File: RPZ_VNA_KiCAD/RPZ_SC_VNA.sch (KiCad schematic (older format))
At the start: 47 parts, among them J1 GPIO Header, J2 Signal_Out, P1 Input, P2 Output, U1 SI5351A, U2 NL7WB66, U3 NL7WB66, U4 OPAMP, U5 OPAMP, Y1 CX3225

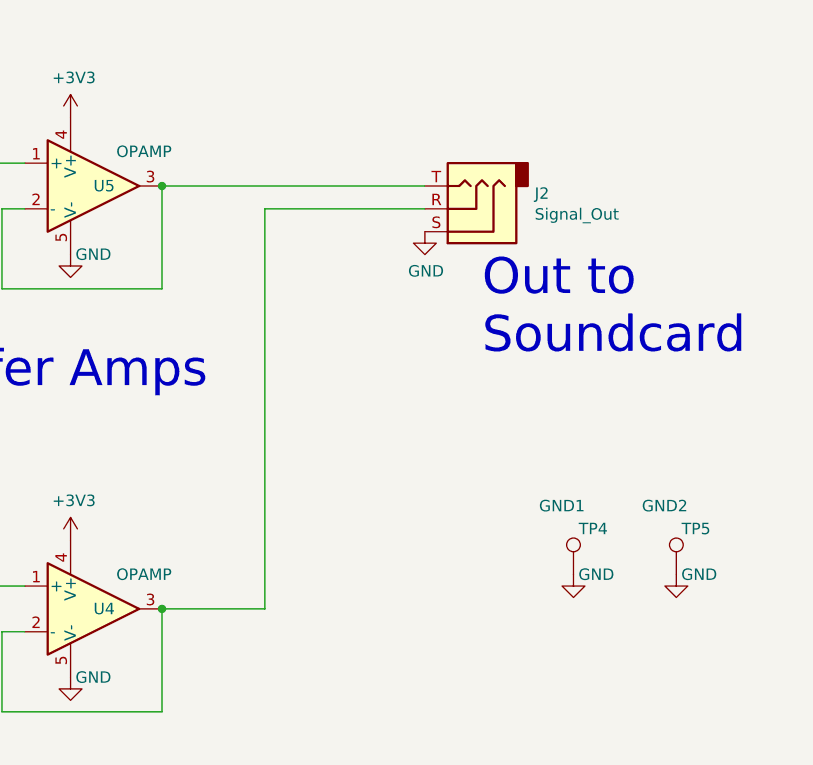
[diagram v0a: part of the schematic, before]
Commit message: Flipped Audio Jack, put Test on Tip, Ref on Ring
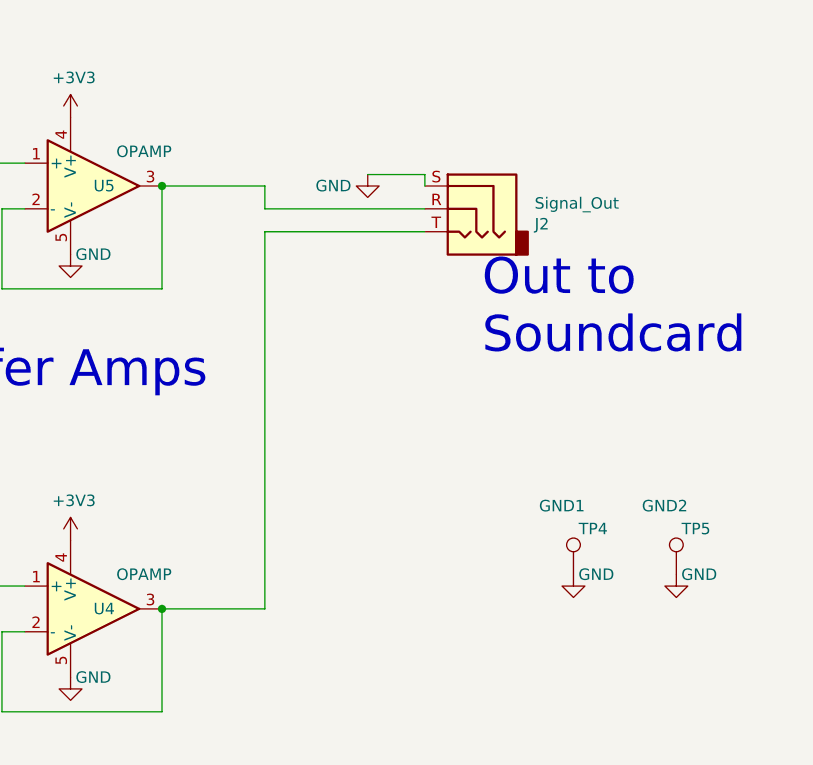
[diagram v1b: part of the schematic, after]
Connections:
- net at U4.2 (-), U4.3: now also J2.T; no longer J2.R
- net at U5.2 (-), U5.3: now also J2.R; no longer J2.T
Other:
- moved on the sheet: J2
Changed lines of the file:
@@
 F 3 "~" H 9350 4200 50  0001 C CNN
 	1    9350 4200
-	-1   0    0    1
+	-1   0    0    -1
 $EndComp
 $Comp
 L power:GND #PWR036
 U 1 1 5D164434
-P 9150 4300
-F 0 "#PWR036" H 9150 4050 50  0001 C CNN
-F 1 "GND" H 9155 4127 50  0000 C CNN
-F 2 "" H 9150 4300 50  0001 C CNN
-F 3 "" H 9150 4300 50  0001 C CNN
-	1    9150 4300
-	1    0    0    -1
-$EndComp
-Wire Wire Line
-	8000 4100 9150 4100
-Connection ~ 8000 4100
-Wire Wire Line
-	9150 4200 8450 4200
-Wire Wire Line
-	8450 4200 8450 5950
+P 8900 4050
+F 0 "#PWR036" H 8900 3800 50  0001 C CNN
+F 1 "GND" H 8750 4000 50  0000 C CNN
+F 2 "" H 8900 4050 50  0001 C CNN
+F 3 "" H 8900 4050 50  0001 C CNN
+	1    8900 4050
+	1    0    0    -1
+$EndComp
 $Comp
 L power:GND #PWR032
@@
 Wire Wire Line
 	3150 1450 3800 1450
+Wire Wire Line
+	8450 4300 9150 4300
+Wire Wire Line
+	8450 4300 8450 5950
+Wire Wire Line
+	9150 4200 8450 4200
+Wire Wire Line
+	8450 4200 8450 4100
+Wire Wire Line
+	8450 4100 8000 4100
+Connection ~ 8000 4100
+Wire Wire Line
+	8900 4050 9150 4050
+Wire Wire Line
+	9150 4050 9150 4100
 $EndSCHEMATC

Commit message: Actually pushing the changes, forgot to hit Ctrl-S
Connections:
- net +3V3: no longer U4.4 (V+), U5.4 (V+)
- net +5V: now reaches J1.2 (Pin_2)
- net +5V: now also J1.4 (Pin_4), U4.4 (V+), U5.4 (V+)
- no-connect marks 34 -> 32
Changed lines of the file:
@@
-$EndComp
-$Comp
-L power:+3V3 #PWR031
-U 1 1 5D174116
-P 7600 5650
-F 0 "#PWR031" H 7600 5500 50  0001 C CNN
-F 1 "+3V3" H 7615 5823 50  0000 C CNN
-F 2 "" H 7600 5650 50  0001 C CNN
-F 3 "" H 7600 5650 50  0001 C CNN
-	1    7600 5650
-	1    0    0    -1
-$EndComp
-$Comp
-L power:+3V3 #PWR033
-U 1 1 5D17682F
-P 7600 3800
-F 0 "#PWR033" H 7600 3650 50  0001 C CNN
-F 1 "+3V3" H 7615 3973 50  0000 C CNN
-F 2 "" H 7600 3800 50  0001 C CNN
-F 3 "" H 7600 3800 50  0001 C CNN
-	1    7600 3800
-	1    0    0    -1
 $EndComp
 $Comp
@@
 Wire Wire Line
 	9200 1650 9550 1650
-NoConn ~ 10050 1250
-NoConn ~ 10050 1350
 NoConn ~ 9550 1550
 NoConn ~ 10050 1550
@@
 NoConn ~ 9550 1850
 NoConn ~ 9550 1750
-Wire Wire Line
-	10050 1450 10300 1450
 $Comp
 L power:GND #PWR039
 U 1 1 5D18E6DE
-P 10300 1450
-F 0 "#PWR039" H 10300 1200 50  0001 C CNN
-F 1 "GND" H 10305 1277 50  0000 C CNN
-F 2 "" H 10300 1450 50  0001 C CNN
-F 3 "" H 10300 1450 50  0001 C CNN
-	1    10300 1450
+P 10800 1550
+F 0 "#PWR039" H 10800 1300 50  0001 C CNN
+F 1 "GND" H 10805 1377 50  0000 C CNN
+F 2 "" H 10800 1550 50  0001 C CNN
+F 3 "" H 10800 1550 50  0001 C CNN
+	1    10800 1550
 	1    0    0    -1
 $EndComp
@@
 L power:PWR_FLAG #FLG0101
 U 1 1 5D1FA915
-P 10300 1450
-F 0 "#FLG0101" H 10300 1525 50  0001 C CNN
-F 1 "PWR_FLAG" H 10300 1623 50  0000 C CNN
-F 2 "" H 10300 1450 50  0001 C CNN
-F 3 "~" H 10300 1450 50  0001 C CNN
-	1    10300 1450
-	1    0    0    -1
-$EndComp
-Connection ~ 10300 1450
+P 10800 1550
+F 0 "#FLG0101" H 10800 1625 50  0001 C CNN
+F 1 "PWR_FLAG" H 10800 1723 50  0000 C CNN
+F 2 "" H 10800 1550 50  0001 C CNN
+F 3 "~" H 10800 1550 50  0001 C CNN
+	1    10800 1550
+	1    0    0    -1
+$EndComp
+Connection ~ 10800 1550
 $Comp
 L power:GND #PWR0101
@@
 Wire Wire Line
 	9150 4050 9150 4100
+$Comp
+L power:+5V #PWR?
+U 1 1 5CDD2C36
+P 7600 3800
+F 0 "#PWR?" H 7600 3650 50  0001 C CNN
+F 1 "+5V" H 7615 3973 50  0000 C CNN
+F 2 "" H 7600 3800 50  0001 C CNN
+F 3 "" H 7600 3800 50  0001 C CNN
+	1    7600 3800
+	1    0    0    -1
+$EndComp
+$Comp
+L power:+5V #PWR?
+U 1 1 5CDDE1F7
+P 10200 1250
+F 0 "#PWR?" H 10200 1100 50  0001 C CNN
+F 1 "+5V" H 10215 1423 50  0000 C CNN
+F 2 "" H 10200 1250 50  0001 C CNN
+F 3 "" H 10200 1250 50  0001 C CNN
+	1    10200 1250
+	1    0    0    -1
+$EndComp
+Wire Wire Line
+	10050 1350 10200 1350
+Wire Wire Line
+	10200 1350 10200 1250
+Wire Wire Line
+	10200 1250 10050 1250
+Connection ~ 10200 1250
+$Comp
+L power:PWR_FLAG #FLG?
+U 1 1 5CDE8352
+P 10550 1250
+F 0 "#FLG?" H 10550 1325 50  0001 C CNN
+F 1 "PWR_FLAG" H 10550 1423 50  0000 C CNN
+F 2 "" H 10550 1250 50  0001 C CNN
+F 3 "~" H 10550 1250 50  0001 C CNN
+	1    10550 1250
+	1    0    0    -1
+$EndComp
+Wire Wire Line
+	10200 1250 10550 1250
+Wire Wire Line
+	10200 1550 10200 1450
+Wire Wire Line
+	10200 1450 10050 1450
+Wire Wire Line
+	10200 1550 10800 1550
+$Comp
+L power:+5V #PWR?
+U 1 1 5CDFAB83
+P 7600 5650
+F 0 "#PWR?" H 7600 5500 50  0001 C CNN
+F 1 "+5V" H 7615 5823 50  0000 C CNN
+F 2 "" H 7600 5650 50  0001 C CNN
+F 3 "" H 7600 5650 50  0001 C CNN
+	1    7600 5650
+	1    0    0    -1
+$EndComp
 $EndSCHEMATC

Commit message: Built PCB, has conflicts with Raspberry Pi Zero Footprint. Smaller Pads and maybe increase size of PCB
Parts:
- removed U4, U5: OPAMP, symbol pspice:OPAMP
- added U4: LM2904, Package_SO:SO-8_3.9x4.9mm_P1.27mm, symbol Amplifier_Operational:LM2904
- C1, C10, C11, C12, C13, C14, C15, C2, C3, C4, C5, C6, C7, C8, C9: footprint (none) -> Capacitor_SMD:C_0805_2012Metric
- Input1: renamed from P1; value Input -> P1; footprint (none) -> SMA:SMA_EDGE
- J2: footprint (none) -> Connector_Audio:Jack_3.5mm_CUI_SJ-3523-SMT_Horizontal
- L1, L2: footprint (none) -> Inductor_SMD:L_0805_2012Metric
- Output1: renamed from P2; value Output -> P2; footprint (none) -> SMA:SMA_EDGE
- R1, R10, R11, R12, R13, R14, R15, R2, R3, R4, R5, R6, R7, R8, R9: footprint (none) -> Resistor_SMD:R_0805_2012Metric
- TP1, TP2, TP3, TP4, TP5: footprint (none) -> TestPoint:TestPoint_Plated_Hole_D2.0mm
- U2, U3: footprint (none) -> SMA:VFSOP-8
- Y1: footprint (none) -> SMA:CX3225
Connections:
- net +5V: now also U4.8 (V+)
- net GND: now also U4.4 (V-)
- net at C12.1, R10.2: now also U4.5 (+)
- net at J2.T: now also U4.6 (-), U4.7
- net at C14.1, R12.2: now also U4.3 (+)
- net at J2.R: now also U4.1, U4.2 (-)

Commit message: Finished PCB 1.0 and created respective gerber files and zipped 'em
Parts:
- J2: footprint Connector_Audio:Jack_3.5mm_CUI_SJ-3523-SMT_Horizontal -> SMA:Tayda_3.5mm_stereo_TRS_jack_A-853; symbol Connector:AudioJack3 -> Connector_edit:AudioJack3
- TP1, TP2, TP3, TP4, TP5: footprint TestPoint:TestPoint_Plated_Hole_D2.0mm -> TestPoint:TestPoint_THTPad_D1.0mm_Drill0.5mm
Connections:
- net GND: now also J2.1 (S); no longer J2.S
- net at U4.1, U4.2 (-): now also J2.3 (R); no longer J2.R
- net at U4.6 (-), U4.7: now also J2.2 (T); no longer J2.T
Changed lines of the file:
@@
 RPi-Zero GPIO
 $Comp
-L Connector:AudioJack3 J2
+L Connector_edit:AudioJack3 J2
 U 1 1 5D154F76
 P 9350 4200
 F 0 "J2" H 9070 4133 50  0000 R CNN
 F 1 "Signal_Out" H 9070 4224 50  0000 R CNN
-F 2 "Connector_Audio:Jack_3.5mm_CUI_SJ-3523-SMT_Horizontal" H 9350 4200 50  0001 C CNN
+F 2 "SMA:Tayda_3.5mm_stereo_TRS_jack_A-853" H 9350 4200 50  0001 C CNN
 F 3 "~" H 9350 4200 50  0001 C CNN
 	1    9350 4200
@@
 F 0 "TP3" H 3350 1850 50  0000 R CNN
 F 1 "LO_I" H 3142 1867 50  0000 R CNN
-F 2 "TestPoint:TestPoint_Plated_Hole_D2.0mm" H 3400 1750 50  0001 C CNN
+F 2 "TestPoint:TestPoint_THTPad_D1.0mm_Drill0.5mm" H 3400 1750 50  0001 C CNN
 F 3 "~" H 3400 1750 50  0001 C CNN
 	1    3200 1750
@@
 F 0 "TP2" H 3150 1650 50  0000 L CNN
 F 1 "REF" H 3200 1550 50  0000 L CNN
-F 2 "TestPoint:TestPoint_Plated_Hole_D2.0mm" H 3350 1450 50  0001 C CNN
+F 2 "TestPoint:TestPoint_THTPad_D1.0mm_Drill0.5mm" H 3350 1450 50  0001 C CNN
 F 3 "~" H 3350 1450 50  0001 C CNN
 	1    3150 1450
@@
 F 0 "TP1" H 2050 6400 50  0000 R CNN
 F 1 "Test_IN" H 1950 6500 50  0000 R CNN
-F 2 "TestPoint:TestPoint_Plated_Hole_D2.0mm" H 2100 6200 50  0001 C CNN
+F 2 "TestPoint:TestPoint_THTPad_D1.0mm_Drill0.5mm" H 2100 6200 50  0001 C CNN
 F 3 "~" H 2100 6200 50  0001 C CNN
 	1    1900 6200
@@
 F 0 "TP5" H 10400 6000 50  0000 R CNN
 F 1 "GND2" H 10300 6100 50  0000 R CNN
-F 2 "TestPoint:TestPoint_Plated_Hole_D2.0mm" H 10450 5800 50  0001 C CNN
+F 2 "TestPoint:TestPoint_THTPad_D1.0mm_Drill0.5mm" H 10450 5800 50  0001 C CNN
 F 3 "~" H 10450 5800 50  0001 C CNN
 	1    10250 5800
@@
 F 0 "TP4" H 9950 6000 50  0000 R CNN
 F 1 "GND1" H 9850 6100 50  0000 R CNN
-F 2 "TestPoint:TestPoint_Plated_Hole_D2.0mm" H 10000 5800 50  0001 C CNN
+F 2 "TestPoint:TestPoint_THTPad_D1.0mm_Drill0.5mm" H 10000 5800 50  0001 C CNN
 F 3 "~" H 10000 5800 50  0001 C CNN
 	1    9800 5800
